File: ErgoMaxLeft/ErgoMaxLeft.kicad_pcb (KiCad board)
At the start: 2 copper layers, 92 parts, among them J1 AudioJack4_Ground, K1 KEYSW, K10 KEYSW, K11 KEYSW, K12 KEYSW, K13 KEYSW, K14 KEYSW, K15 KEYSW, K16 KEYSW, K17 KEYSW, K18 KEYSW, K19 KEYSW, K2 KEYSW, K20 KEYSW, K21 KEYSW, K22 KEYSW, K23 KEYSW, K24 KEYSW, K25 KEYSW, K26 KEYSW, K27 KEYSW, K28 KEYSW, K29 KEYSW, K3 KEYSW, K30 KEYSW, K31 KEYSW, K32 KEYSW, K33 KEYSW, K34 KEYSW, K35 KEYSW, K36 KEYSW, K37 KEYSW, K38 KEYSW, K39 KEYSW, K4 KEYSW, K40 KEYSW, K41 KEYSW, K42 KEYSW, K43 KEYSW, K44 KEYSW, K5 KEYSW, K6 KEYSW, K7 KEYSW, K8 KEYSW, K9 KEYSW, U1 ProMicro

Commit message: WIP PCB - add 2 cutouts
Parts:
- moved U1 173.1 mm to (236.3, 40.7)
- moved D43 39.6 mm to (255.6, 189.3)
- moved K35 39.6 mm to (243.9, 133.2)
- moved K38 39.6 mm to (148.6, 158.9)
- moved D1 39.6 mm to (158.3, 69.8)
- moved D8 39.6 mm to (158.3, 88.9)
- moved K13 39.6 mm to (243.9, 80.8)
- moved K18 39.6 mm to (205.7, 98.5)
- moved K21 39.6 mm to (124.8, 120.8)
- moved K37 39.6 mm to (129.6, 158.9)
- moved K8 39.6 mm to (148.6, 82.7)
- moved D11 39.6 mm to (215.2, 85.7)
- moved D15 39.6 mm to (158.3, 108.1)
- moved D2 39.6 mm to (177.2, 66.7)
- moved D21 39.6 mm to (139.1, 127.0)
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
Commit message: WIP PCB - make rough cutout so Kicad doesn't complain anymore, add 2 mounting holes
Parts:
- added ?: , MountingHole:MountingHole_6.4mm_M6, F.Cu at (115.1, 156.6)
- added ?: , MountingHole:MountingHole_6.5mm_Pad, F.Cu at (256.6, 137.3)
- moved J1 147.3 mm to (138.3, 45.8)
- moved R1 147.3 mm to (156.5, 43.4)
- moved R2 147.3 mm to (156.5, 41.2)
- moved D44 7.80 mm to (270.3, 198.3)
- moved D20 7.21 mm to (249.8, 112.2)
- moved D13 3.70 mm to (249.8, 87.7)
- moved D6 3.39 mm to (250.1, 68.0)
- moved D35 2.34 mm to (251.2, 139.0)
- moved D36 2.15 mm to (276.4, 186.8)
- moved D37 2.07 mm to (139.1, 162.9)
- moved D38 2.04 mm to (158.2, 163.0)
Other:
- board outline added: 182.8 x 178.9 mm
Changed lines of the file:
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@@
   (general
     (thickness 1.6)
-    (drawings 1)
+    (drawings 13)
     (tracks 0)
     (zones 0)
-    (modules 92)
+    (modules 94)
     (nets 67)
   )
@@
     (zone_45_only no)
     (trace_min 0.2)
-    (segment_width 0.2)
+    (segment_width 0.381)
     (edge_width 0.381)
     (via_size 0.8)
@@
     (mod_text_size 1 1)
     (mod_text_width 0.15)
-    (pad_size 1.524 1.524)
-    (pad_drill 0.762)
+    (pad_size 6.3754 6.3754)
+    (pad_drill 6.3754)
     (pad_to_mask_clearance 0.051)
     (solder_mask_min_width 0.25)
@@
     (add_net VCC)
   )
+  (module MountingHole:MountingHole_6.4mm_M6 (layer F.Cu)
+    (at 115.06 156.62)
+    (descr "Mounting Hole 6.4mm, no annular, M6")
+    (tags "mounting hole 6.4mm no annular m6")
+    (attr virtual)
+    (fp_text reference "" (at 0 -7.4) (layer F.SilkS) hide
+      (effects (font (size 1 1) (thickness 0.15)))
+    )
+    (fp_text value "" (at 0 7.4) (layer F.Fab) hide
+      (effects (font (size 1 1) (thickness 0.15)))
+    )
+    (fp_circle (center 0 0) (end 6.65 0) (layer F.CrtYd) (width 0.05))
+    (fp_circle (center 0 0) (end 6.4 0) (layer Cmts.User) (width 0.15))
+    (fp_text user %R (at 0.3 0) (layer F.Fab)
+      (effects (font (size 1 1) (thickness 0.15)))
+    )
+    (pad "" np_thru_hole circle (at 0 0) (size 6.3754 6.3754) (drill 6.3754) (layers *.Cu *.Mask)
+      (solder_mask_margin -0.254) (zone_connect 2))
+  )
   (module Keebio-Parts:Diode (layer F.Cu)
     (at 158.27232 69.82076 90)
@@
   )
   (module Keebio-Parts:Diode (layer F.Cu)
-    (at 253.4766 67.9056 90)
+    (at 250.09 67.99 90)
     (fp_text reference D6 (at 0 0 90) (layer F.SilkS)
       (effects (font (size 1.27 1.524) (thickness 0.2032)))
@@
   )
   (module Keebio-Parts:Diode (layer F.Cu)
-    (at 253.45628 86.96068 90)
+    (at 249.83 87.71 90)
     (fp_text reference D13 (at 0 0 90) (layer F.SilkS)
       (effects (font (size 1.27 1.524) (thickness 0.2032)))
@@
   )
   (module Keebio-Parts:Diode (layer F.Cu)
-    (at 253.4512 106.04624 90)
+    (at 249.75 112.23 90)
     (fp_text reference D20 (at 0 0.133399 90) (layer F.SilkS)
       (effects (font (size 1.27 1.524) (thickness 0.2032)))
@@
   )
   (module Keebio-Parts:Diode (layer F.Cu)
-    (at 253.4866 139.39206 90)
+    (at 251.18 138.99 90)
     (fp_text reference D35 (at 0 0 90) (layer F.SilkS)
       (effects (font (size 1.27 1.524) (thickness 0.2032)))
@@
   )
   (module Keebio-Parts:Diode (layer F.Cu)
-    (at 277.00954 188.8992 65)
+    (at 276.42 186.83 65)
     (fp_text reference D36 (at 0 0 65) (layer F.SilkS)
       (effects (font (size 1.27 1.524) (thickness 0.2032)))
@@
   )
   (module Keebio-Parts:Diode (layer F.Cu)
-    (at 139.0469 165.0232 90)
+    (at 139.06 162.95 90)
     (fp_text reference D37 (at 0 0 90) (layer F.SilkS)
       (effects (font (size 1.27 1.524) (thickness 0.2032)))
@@
   )
   (module Keebio-Parts:Diode (layer F.Cu)
-    (at 158.1858 165.074 90)
+    (at 158.18 163.03 90)
     (fp_text reference D38 (at 0 0 90) (layer F.SilkS)
       (effects (font (size 1.27 1.524) (thickness 0.2032)))
@@
   )
   (module Keebio-Parts:Diode (layer F.Cu)
-    (at 269.02124 206.00356 65)
+    (at 270.349824 198.313033 65)
     (fp_text reference D44 (at 0 0 65) (layer F.SilkS)
       (effects (font (size 1.27 1.524) (thickness 0.2032)))
@@
   )
   (module Keebio-Parts:4pin35mmAudio (layer F.Cu)
-    (at 53.30298 166.14516)
+    (at 138.30298 45.84516)
     (fp_text reference J1 (at 1.27 0 90) (layer F.SilkS) hide
       (effects (font (size 1.524 1.778) (thickness 0.3048)))
@@
   )
   (module Keebio-Parts:Resistor (layer F.Cu)
-    (at 71.45848 163.693261)
+    (at 156.45848 43.393261)
     (fp_text reference R1 (at 0 0) (layer F.SilkS) hide
       (effects (font (size 1 1) (thickness 0.2)))
@@
   )
   (module Keebio-Parts:Resistor (layer F.Cu)
-    (at 71.45848 161.543261)
+    (at 156.45848 41.243261)
     (fp_text reference R2 (at 0 0) (layer F.SilkS) hide
       (effects (font (size 1 1) (thickness 0.2)))
@@
       (net 62 "Net-(U1-Pad1)"))
   )
-  (gr_line (start 111.86 60.62) (end 111.86 168.57) (layer Edge.Cuts) (width 0.381))
+  (module MountingHole:MountingHole_6.5mm_Pad (layer F.Cu)
+    (at 256.589625 137.335287)
+    (descr "Mounting Hole 6.5mm")
+    (tags "mounting hole 6.5mm")
+    (attr virtual)
+    (fp_text reference "" (at 0 -7.5) (layer F.SilkS) hide
+      (effects (font (size 1 1) (thickness 0.15)))
+    )
+    (fp_text value "" (at 0 7.5) (layer F.Fab) hide
+      (effects (font (size 1 1) (thickness 0.15)))
+    )
+    (fp_circle (center 0 0) (end 6.75 0) (layer F.CrtYd) (width 0.05))
+    (fp_circle (center 0 0) (end 6.5 0) (layer Cmts.User) (width 0.15))
+    (fp_text user %R (at 0.3 0) (layer F.Fab)
+      (effects (font (size 1 1) (thickness 0.15)))
+    )
+    (pad "" np_thru_hole circle (at 0 0) (size 6.3754 6.3754) (drill 6.3754) (layers *.Cu *.Mask)
+      (solder_mask_margin -0.254))
+  )
+  (gr_line (start 253.65 137.29) (end 258.55 137.33) (layer Edge.Cuts) (width 0.381))
+  (gr_line (start 116.72 27.25) (end 110.34 51.1) (layer Edge.Cuts) (width 0.381))
+  (gr_line (start 250.48 26.14) (end 116.72 27.26) (layer Edge.Cuts) (width 0.381))
+  (gr_line (start 253.65 29.33) (end 250.475 26.155) (layer Edge.Cuts) (width 0.381))
+  (gr_line (start 253.65 29.34) (end 253.65 137.29) (layer Edge.Cuts) (width 0.381))
+  (gr_line (start 110.34 159.05) (end 119.865 168.575) (layer Edge.Cuts) (width 0.381))
+  (gr_line (start 291.63972 152.7635) (end 258.5486 137.333) (layer Edge.Cuts) (width 0.381))
+  (gr_line (start 293.17642 156.98244) (end 291.63972 152.7635) (layer Edge.Cuts) (width 0.381))
+  (gr_line (start 271.49244 203.48476) (end 293.17642 156.98244) (layer Edge.Cuts) (width 0.381))
+  (gr_line (start 267.2735 205.01892) (end 271.49244 203.48476) (layer Edge.Cuts) (width 0.381))
+  (gr_line (start 189.105 168.575) (end 267.2735 205.01892) (layer Edge.Cuts) (width 0.381))
+  (gr_line (start 119.865 168.575) (end 189.105 168.575) (layer Edge.Cuts) (width 0.381))
+  (gr_line (start 110.34 51.1) (end 110.34 159.05) (layer Edge.Cuts) (width 0.381))
 )

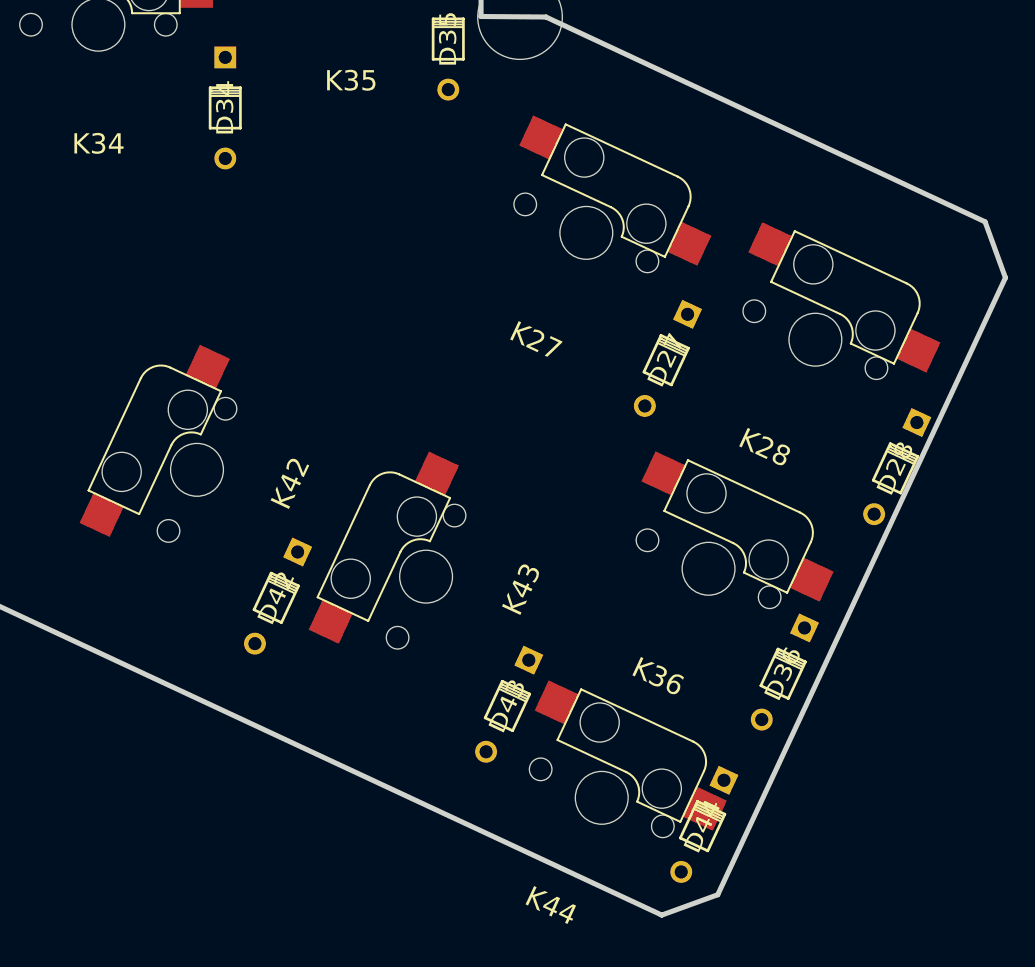
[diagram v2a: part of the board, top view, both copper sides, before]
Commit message: WIP PCB - fix placement of thumb switch sockets
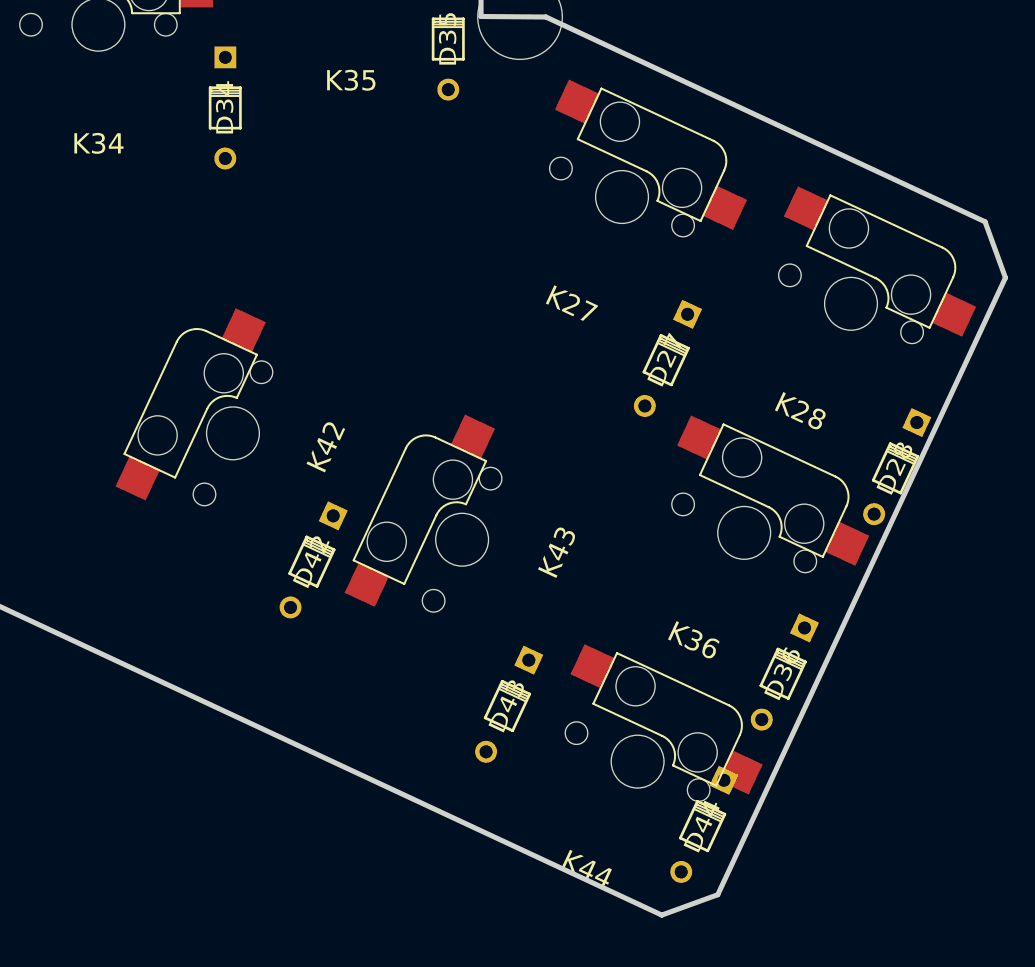
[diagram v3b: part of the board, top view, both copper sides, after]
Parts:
- moved K43 3.89 mm to (252.2, 176.7)
- moved K42 3.86 mm to (235.0, 168.7)
- moved K44 3.84 mm to (265.5, 193.5)
- moved D42 3.82 mm to (240.9, 178.4)
- moved K27 3.81 mm to (264.3, 150.9)
- moved K36 3.81 mm to (273.5, 176.2)
- moved K28 3.81 mm to (281.5, 158.9)
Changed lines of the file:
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@@
   )
   (module Keebio-Parts:Diode (layer F.Cu)
-    (at 238.21866 181.10648 65)
+    (at 240.9 178.38 65)
     (fp_text reference D42 (at 0 0 65) (layer F.SilkS)
       (effects (font (size 1.27 1.524) (thickness 0.2032)))
@@
   )
   (module keyboard_parts:Kailh_MX_Socket (layer F.Cu)
-    (at 261.584906 153.599594 335)
+    (at 264.274894 150.896396 335)
     (fp_text reference K27 (at 0 9 335) (layer F.SilkS)
       (effects (font (size 1.524 1.524) (thickness 0.3048)))
@@
   )
   (module keyboard_parts:Kailh_MX_Socket (layer F.Cu)
-    (at 278.850069 161.650471 335)
+    (at 281.534682 158.946393 335)
     (fp_text reference K28 (at 0 9 335) (layer F.SilkS)
       (effects (font (size 1.524 1.524) (thickness 0.3048)))
@@
   )
   (module keyboard_parts:Kailh_MX_Socket (layer F.Cu)
-    (at 270.799192 178.915634 335)
+    (at 273.483805 176.211556 335)
     (fp_text reference K36 (at 0 9 335) (layer F.SilkS)
       (effects (font (size 1.524 1.524) (thickness 0.3048)))
@@
       (effects (font (size 1.524 1.524) (thickness 0.3048)) (justify mirror))
     )
-    (fp_line (start -7.62 5.62) (end -7.62 7.62) (layer Dwgs.User) (width 0.381))
-    (fp_line (start 5.62 -7.62) (end 7.62 -7.62) (layer Dwgs.User) (width 0.381))
-    (fp_line (start 7.62 5.62) (end 7.62 7.62) (layer Dwgs.User) (width 0.381))
-    (fp_line (start 5.62 7.62) (end 7.62 7.62) (layer Dwgs.User) (width 0.381))
-    (fp_line (start 0.865 -2.54) (end -4.865 -2.54) (layer F.SilkS) (width 0.15))
-    (fp_arc (start 0.865 -0.865) (end 0.865 -2.54) (angle 90) (layer F.SilkS) (width 0.15))
-    (fp_arc (start 4.46 -5.08) (end 4.46 -6.755) (angle 90) (layer F.SilkS) (width 0.15))
-    (fp_line (start 4.46 -6.755) (end -4.865 -6.755) (layer F.SilkS) (width 0.15))
-    (fp_line (start -4.865 -6.75) (end -4.865 -2.54) (layer F.SilkS) (width 0.15))
-    (fp_line (start 6.135 -5.08) (end 6.135 -0.865) (layer F.SilkS) (width 0.15))
-    (fp_line (start 6.135 -0.865) (end 2.54 -0.865) (layer F.SilkS) (width 0.15))
-    (fp_line (start -7.62 -7.62) (end -5.62 -7.62) (layer Dwgs.User) (width 0.381))
-    (fp_line (start 7.62 -7.62) (end 7.62 -5.62) (layer Dwgs.User) (width 0.381))
-    (fp_line (start -7.62 7.62) (end -5.62 7.62) (layer Dwgs.User) (width 0.381))
-    (fp_line (start -7.62 -5.62) (end -7.62 -7.62) (layer Dwgs.User) (width 0.381))
+    (fp_line (start -7.62 -5.62) (end -7.62 -7.62) (layer Dwgs.User) (width 0.381))
+    (fp_line (start -7.62 7.62) (end -5.62 7.62) (layer Dwgs.User) (width 0.381))
+    (fp_line (start 7.62 -7.62) (end 7.62 -5.62) (layer Dwgs.User) (width 0.381))
+    (fp_line (start -7.62 -7.62) (end -5.62 -7.62) (layer Dwgs.User) (width 0.381))
+    (fp_line (start 6.135 -0.865) (end 2.54 -0.865) (layer F.SilkS) (width 0.15))
+    (fp_line (start 6.135 -5.08) (end 6.135 -0.865) (layer F.SilkS) (width 0.15))
+    (fp_line (start -4.865 -6.75) (end -4.865 -2.54) (layer F.SilkS) (width 0.15))
+    (fp_line (start 4.46 -6.755) (end -4.865 -6.755) (layer F.SilkS) (width 0.15))
+    (fp_arc (start 4.46 -5.08) (end 4.46 -6.755) (angle 90) (layer F.SilkS) (width 0.15))
+    (fp_arc (start 0.865 -0.865) (end 0.865 -2.54) (angle 90) (layer F.SilkS) (width 0.15))
+    (fp_line (start 0.865 -2.54) (end -4.865 -2.54) (layer F.SilkS) (width 0.15))
+    (fp_line (start 5.62 7.62) (end 7.62 7.62) (layer Dwgs.User) (width 0.381))
+    (fp_line (start 7.62 5.62) (end 7.62 7.62) (layer Dwgs.User) (width 0.381))
+    (fp_line (start 5.62 -7.62) (end 7.62 -7.62) (layer Dwgs.User) (width 0.381))
+    (fp_line (start -7.62 5.62) (end -7.62 7.62) (layer Dwgs.User) (width 0.381))
+    (pad "" np_thru_hole circle (at 5.08 0 335) (size 1.7 1.7) (drill 1.7) (layers *.Cu *.Mask))
+    (pad "" np_thru_hole circle (at -5.08 0 335) (size 1.7 1.7) (drill 1.7) (layers *.Cu *.Mask))
+    (pad 2 smd rect (at -6.09 -5.08 335) (size 2.55 2.5) (layers F.Cu F.Paste F.Mask)
+      (net 57 /Row4))
+    (pad "" np_thru_hole circle (at 3.81 -2.54 335) (size 2.95 2.95) (drill 2.95) (layers *.Cu *.Mask))
+    (pad "" np_thru_hole circle (at -2.54 -5.08 335) (size 2.95 2.95) (drill 2.95) (layers *.Cu *.Mask))
+    (pad "" np_thru_hole circle (at 0 0 335) (size 3.98018 3.98018) (drill 3.98018) (layers *.Cu *.Mask))
     (pad 1 smd rect (at 7.36 -2.54 335) (size 2.55 2.5) (layers F.Cu F.Paste F.Mask)
       (net 44 "Net-(D36-Pad2)"))
-    (pad "" np_thru_hole circle (at 0 0 335) (size 3.98018 3.98018) (drill 3.98018) (layers *.Cu *.Mask))
-    (pad "" np_thru_hole circle (at -2.54 -5.08 335) (size 2.95 2.95) (drill 2.95) (layers *.Cu *.Mask))
-    (pad "" np_thru_hole circle (at 3.81 -2.54 335) (size 2.95 2.95) (drill 2.95) (layers *.Cu *.Mask))
-    (pad 2 smd rect (at -6.09 -5.08 335) (size 2.55 2.5) (layers F.Cu F.Paste F.Mask)
-      (net 57 /Row4))
-    (pad "" np_thru_hole circle (at -5.08 0 335) (size 1.7 1.7) (drill 1.7) (layers *.Cu *.Mask))
-    (pad "" np_thru_hole circle (at 5.08 0 335) (size 1.7 1.7) (drill 1.7) (layers *.Cu *.Mask))
     (model /Users/cole/git/keyboard_parts.pretty/PG151101S11.step
       (offset (xyz -4.65 6.8 1.8))
@@
   )
   (module keyboard_parts:Kailh_MX_Socket (layer F.Cu)
-    (at 232.242334 171.459487 65)
+    (at 234.952436 168.708408 65)
     (fp_text reference K42 (at 2.066879 6.818639 65) (layer F.SilkS)
       (effects (font (size 1.524 1.524) (thickness 0.3048)))
@@
   )
   (module keyboard_parts:Kailh_MX_Socket (layer F.Cu)
-    (at 249.507497 179.510364 65)
+    (at 252.22308 176.726588 65)
     (fp_text reference K43 (at 2.19733 6.950322 65) (layer F.SilkS)
       (effects (font (size 1.524 1.524) (thickness 0.3048)))
@@
   )
   (module keyboard_parts:Kailh_MX_Socket (layer F.Cu)
-    (at 262.748315 196.180797 335)
+    (at 265.450951 193.451188 335)
     (fp_text reference K44 (at 0 9 335) (layer F.SilkS)
       (effects (font (size 1.524 1.524) (thickness 0.3048)))
